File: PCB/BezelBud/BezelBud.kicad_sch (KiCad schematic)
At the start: 71 parts, among them J1 USB_C_Receptacle_USB2.0_16P, J2 Conn_01x05_Pin, SW1 SW_SPDT, SW2 SW_SPDT, SW3 SW_SPDT, SW4 SW_SPDT, SW5 SW_SPDT, SW6 SW_SPDT, SW7 SW_SPDT, SW8 SW_SPDT, SW9 SW_SPDT, U1 STM32G431CBT6, U2 USBLC6-2SC6, U3 LP5907MFX-3.3, U4 LP5907MFX-3.3, U5 PCM1861DBT, Y1 Crystal_GND24

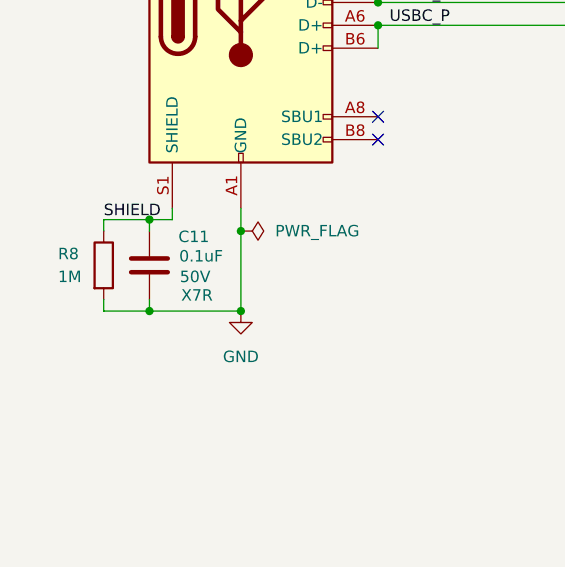
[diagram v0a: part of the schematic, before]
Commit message: removed usb decoupling and moved blink and led vias
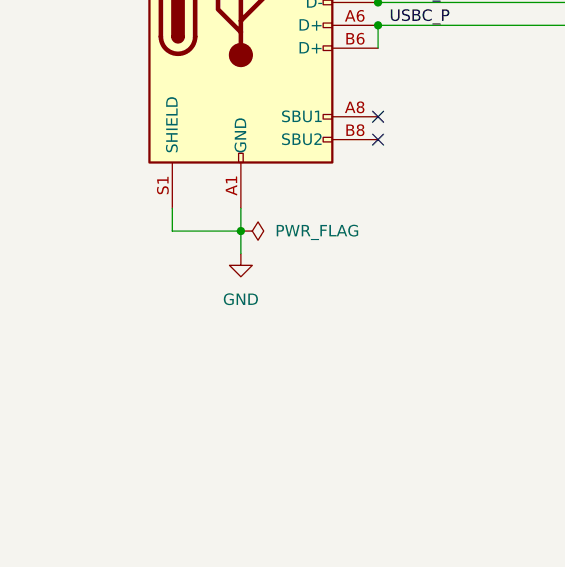
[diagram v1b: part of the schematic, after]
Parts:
- removed C11: 0.1uF, Capacitor_SMD:C_0603_1608Metric, symbol Device:C
- removed R8: 1M, Resistor_SMD:R_0603_1608Metric, symbol Device:R
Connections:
- net SHIELD is gone; now on net GND: J1.S1 (SHIELD)

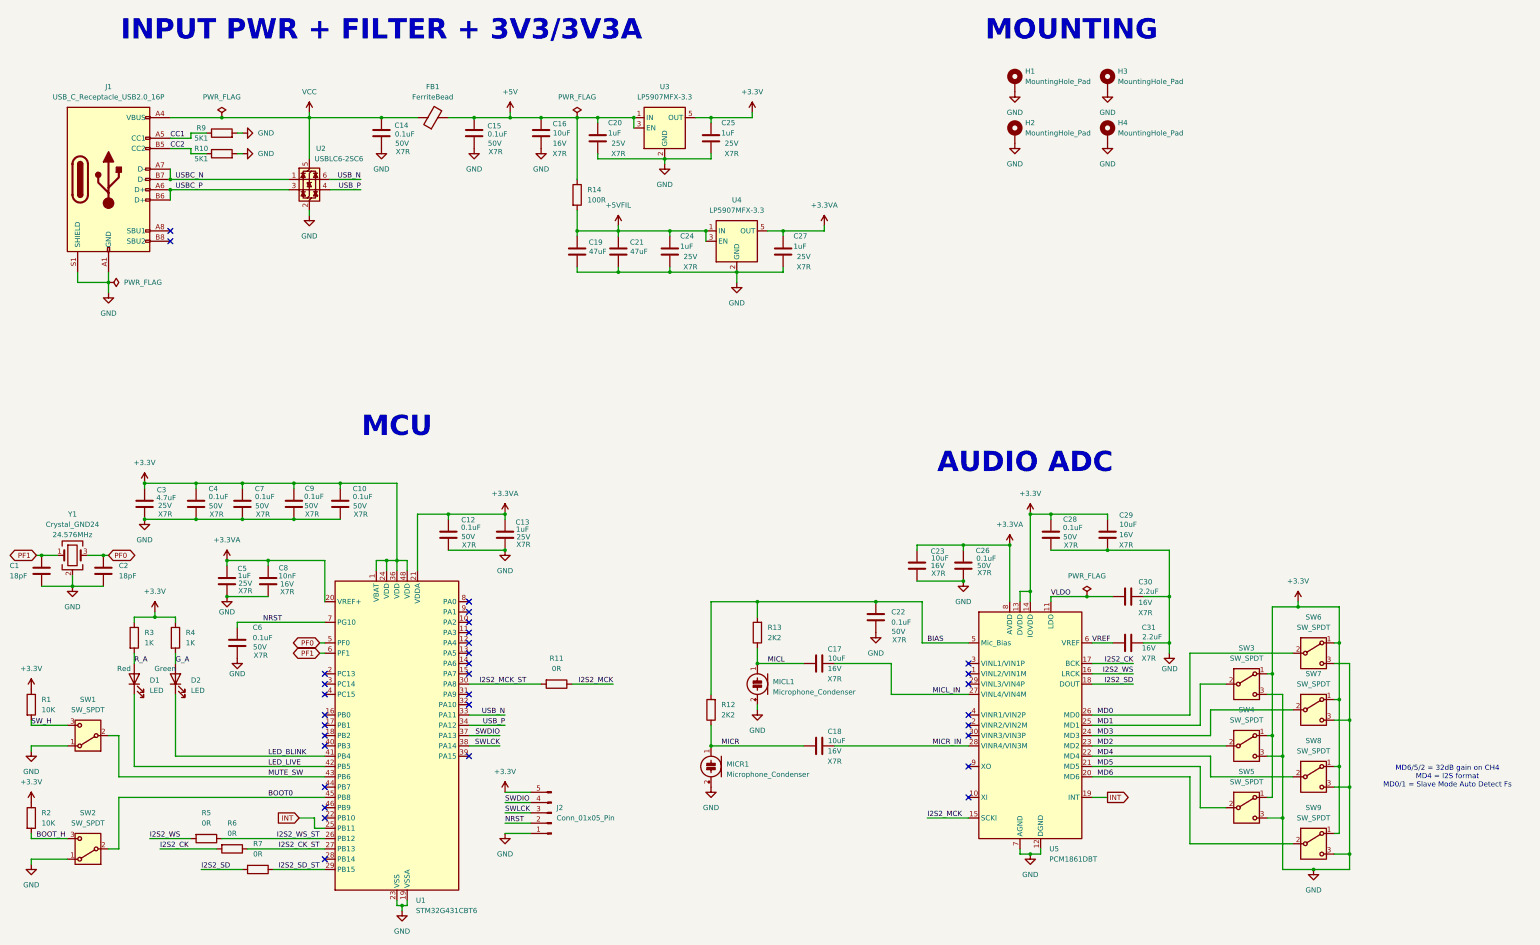
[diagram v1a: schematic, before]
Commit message: Updated to different Mic and finished PCB
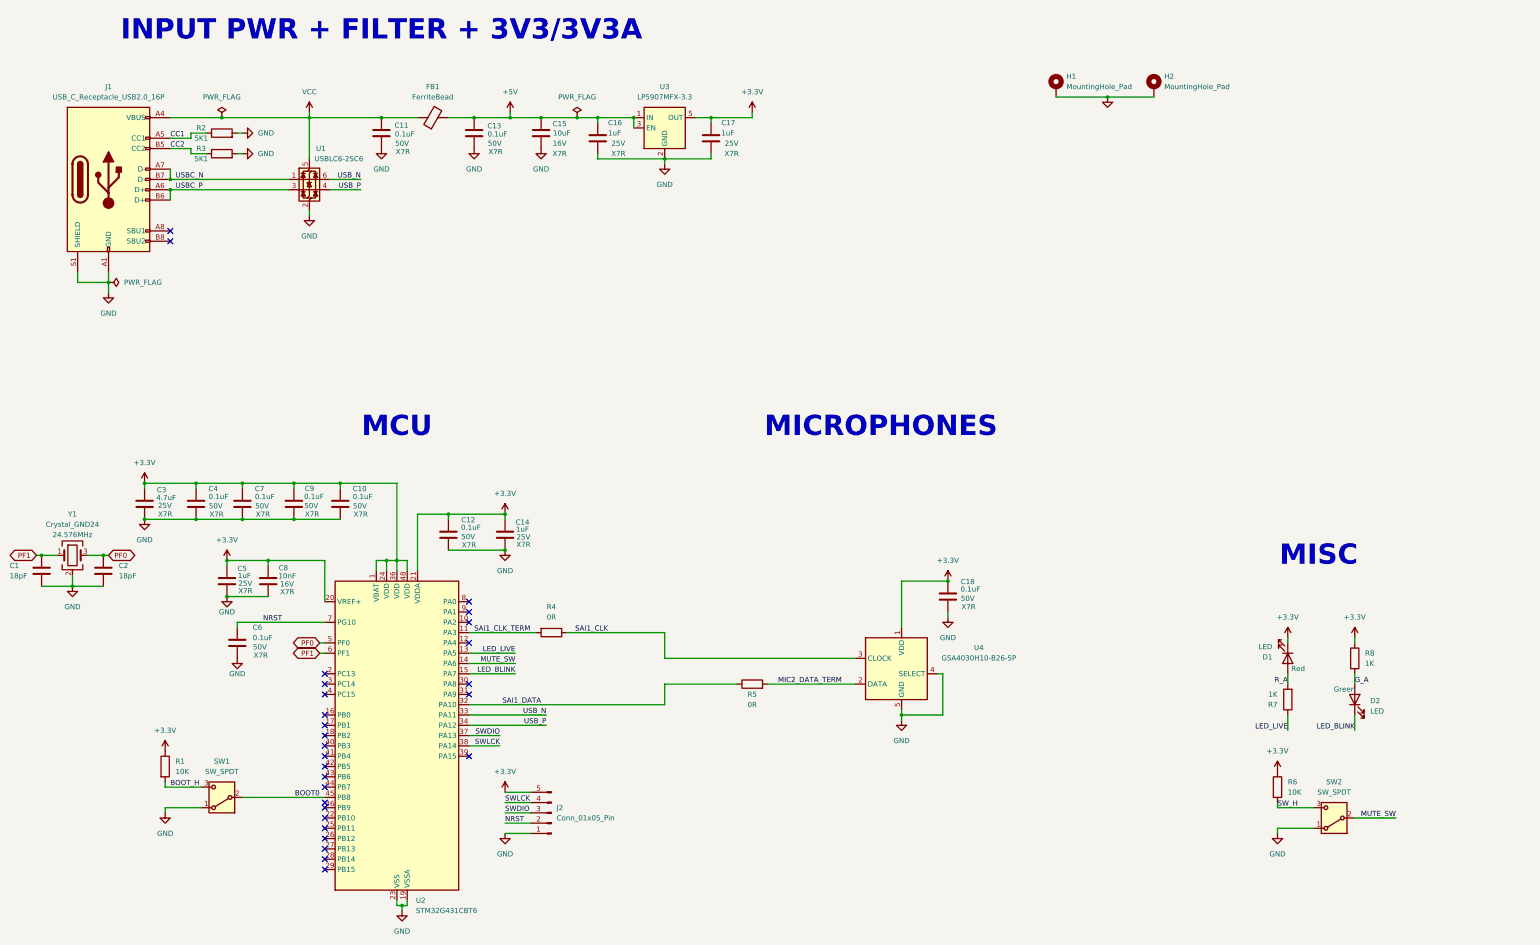
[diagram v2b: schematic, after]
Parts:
- removed C17, C23, C29: 10uF, Capacitor_SMD:C_0805_2012Metric, symbol Device:C
- removed C19, C21: 47uF, Capacitor_SMD:C_1206_3216Metric, symbol Device:C
- removed C22, C26, C28: 0.1uF, Capacitor_SMD:C_0603_1608Metric, symbol Device:C
- removed C24, C27: 1uF, Capacitor_SMD:C_0805_2012Metric, symbol Device:C
- removed C30, C31: 2.2uF, Capacitor_SMD:C_0603_1608Metric, symbol Device:C
- removed H3, H4: MountingHole_Pad, MountingHole:MountingHole_3.2mm_M3_Pad_Via, symbol Mechanical:MountingHole_Pad
- removed MICL1, MICR1: Microphone_Condenser, Resistor_THT:R_Axial_DIN0204_L3.6mm_D1.6mm_P1.90mm_Vertical, symbol Device:Microphone_Condenser
- removed R11, R6, R7: 0R, Resistor_SMD:R_0603_1608Metric, symbol Device:R
- removed R12, R13: 2K2, Resistor_SMD:R_0603_1608Metric, symbol Device:R
- removed R14: 100R, Resistor_SMD:R_0805_2012Metric, symbol Device:R
- removed R4: 1K, Resistor_SMD:R_0603_1608Metric, symbol Device:R
- removed SW3, SW4, SW5, SW6, SW7, SW8, SW9: SW_SPDT, Connector_PinHeader_2.54mm:PinHeader_1x03_P2.54mm_Vertical, symbol Switch:SW_SPDT
- removed U4: LP5907MFX-3.3, Package_TO_SOT_SMD:SOT-23-5, symbol Regulator_Linear:LP5907MFX-3.3
- removed U5: PCM1861DBT, Package_SO:TSSOP-30_4.4x7.8mm_P0.5mm, symbol Audio:PCM1860DBT
- added R5: 0R, Resistor_SMD:R_0603_1608Metric, symbol Device:R
- added R8: 1K, Resistor_SMD:R_0603_1608Metric, symbol Device:R
- added U4: GSA4030H10-B26-5P, BevelBud:GSA4030H10-B26-5P, symbol BevelBud:GSA4030H10-B26-5P
- C18: value 10uF -> 0.1uF; footprint Capacitor_SMD:C_0805_2012Metric -> Capacitor_SMD:C_0603_1608Metric; Voltage 16V -> 50V
- renumbered C14 to C11, C15 to C13, C13 to C14, C16 to C15, C20 to C16, C25 to C17, R2 to R1, R9 to R2, R10 to R3, R5 to R4, R1 to R6, R3 to R7, SW2 to SW1, SW1 to SW2, U2 to U1, U1 to U2
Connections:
- net +3.3VA is gone; now on net +3.3V: C12.1, C14.1, C5.1, C8.1, U2.20 (VREF+), U2.21 (VDDA)
- net I2S2_WS is gone; now on net SAI1_CLK_TERM: R4.2
- net MICR is gone; now on net +3.3V: C18.1
- net MICR_IN is gone; now on net GND: C18.2
- net +3.3V: now also D1.1 (K), R8.1, U4.1 (VDD); no longer R7.1
- net GND: now also U4.4 (SELECT), U4.5 (GND)
- net G_A: now also R8.2
- net LED_BLINK: now also U2.15 (PA7); no longer U2.41 (PB4)
- net LED_LIVE: now also R7.1, U2.13 (PA5); no longer D1.1 (K), U2.42 (PB5)
- net MUTE_SW: now also U2.14 (PA6); no longer U2.43 (PB6)
- net SWDIO: now also J2.3 (Pin_3); no longer J2.4 (Pin_4)
- net SWLCK: now also J2.4 (Pin_4); no longer J2.3 (Pin_3)
- net SAI1_CLK_TERM: now reaches U2.11 (PA3)
- net SAI1_DATA: now reaches U2.32 (PA10)
- net SAI1_DATA: now also R5.1
- net I2S2_CK_ST: no longer names the net of U2.27 (PB13)
- net I2S2_MCK_ST: no longer names the net of U2.30 (PA8)
- net I2S2_SD_ST: no longer names the net of U2.29 (PB15)
- net I2S2_WS_ST: no longer names the net of U2.26 (PB12)
- net I2S2_WS_ST: no longer R4.1
- net INT: no longer names the net of U2.25 (PB11)
- new net MIC2_DATA_TERM: R5.2, U4.2 (DATA)
- new net SAI1_CLK: R4.1, U4.3 (CLOCK)
- no-connect marks 32 -> 28
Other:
- note added: "MICROPHONES"
- note added: "MISC"
- note removed: "AUDIO ADC"
- note removed: "MD6/5/2 = 32dB gain on CH4 MD4 = I2S format MD0/1 = Slave Mode Auto Detect Fs"
- note removed: "MOUNTING"
- moved on the sheet: D1, R1, R4, R6, R7, SW1, SW2

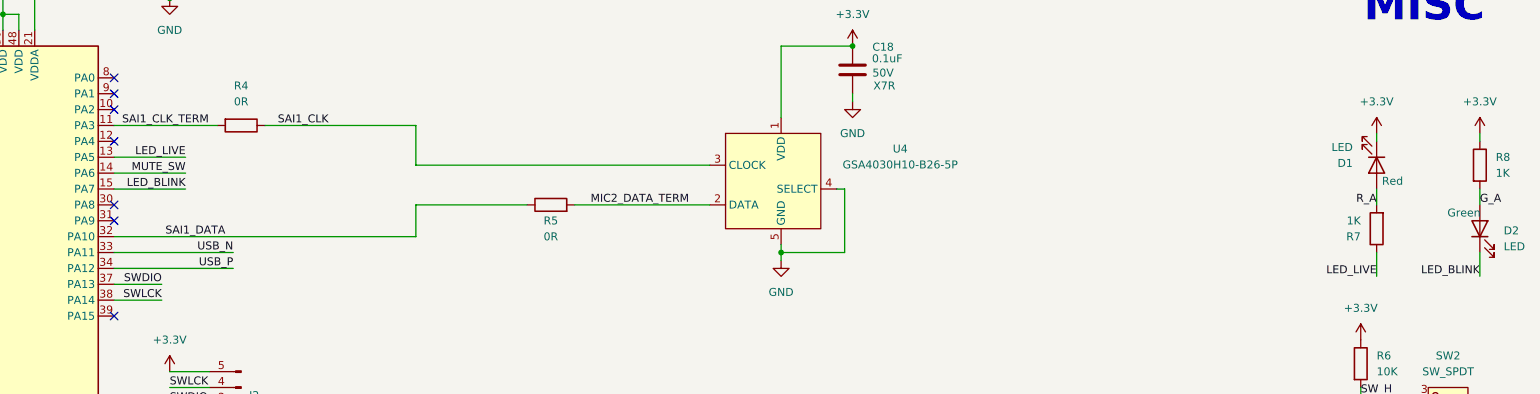
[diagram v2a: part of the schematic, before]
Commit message: deleted gerbers and fixed LED orientation
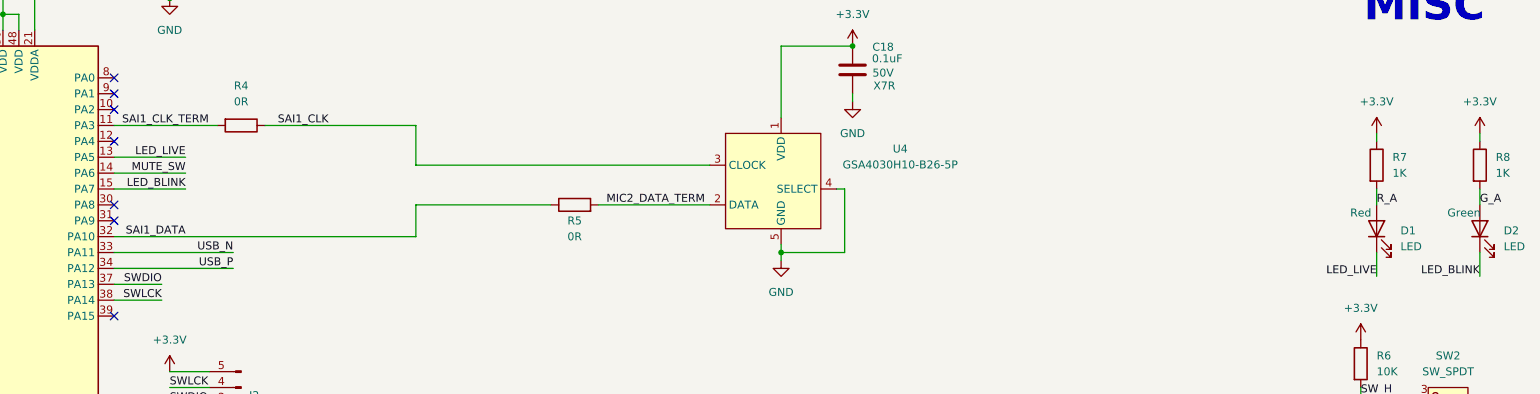
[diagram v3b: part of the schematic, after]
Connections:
- net +3.3V: now also R7.1; no longer D1.1 (K)
- net LED_LIVE: now also D1.1 (K); no longer R7.1
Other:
- moved on the sheet: D1, R5, R7
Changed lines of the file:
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@@
 	(wire
 		(pts
-			(xy 344.17 186.69) (xy 344.17 184.15)
+			(xy 344.17 184.15) (xy 344.17 186.69)
 		)
 		(stroke
@@
 	(wire
 		(pts
-			(xy 190.5 186.69) (xy 208.28 186.69)
+			(xy 190.5 186.69) (xy 212.09 186.69)
 		)
 		(stroke
@@
 	(wire
 		(pts
-			(xy 215.9 186.69) (xy 237.49 186.69)
+			(xy 219.71 186.69) (xy 237.49 186.69)
 		)
 		(stroke
@@
 	)
 	(label "SAI1_DATA"
-		(at 160.02 191.77 180)
+		(at 153.67 191.77 180)
 		(effects
 			(font
@@
 	)
 	(label "MIC2_DATA_TERM"
-		(at 218.44 186.69 0)
+		(at 220.98 186.69 0)
 		(effects
 			(font
@@
 	)
 	(label "R_A"
-		(at 344.17 186.69 180)
+		(at 344.17 186.69 0)
 		(effects
 			(font
 				(size 1.27 1.27)
 			)
-			(justify right bottom)
+			(justify left bottom)
 		)
 	)
@@
 	(symbol
 		(lib_id "Device:R")
-		(at 212.09 186.69 90)
+		(at 215.9 186.69 90)
 		(unit 1)
 		(exclude_from_sim no)
@@
 		(dnp no)
 		(property "Reference" "R5"
-			(at 212.09 189.23 90)
+			(at 215.9 189.23 90)
 			(effects
 				(font
@@
 		)
 		(property "Value" "0R"
-			(at 212.09 191.77 90)
+			(at 215.9 191.77 90)
 			(effects
 				(font
@@
 		)
 		(property "Footprint" "Resistor_SMD:R_0603_1608Metric"
-			(at 212.09 188.468 90)
+			(at 215.9 188.468 90)
 			(effects
 				(font
@@
 		)
 		(property "Datasheet" "~"
-			(at 212.09 186.69 0)
+			(at 215.9 186.69 0)
 			(effects
 				(font
@@
 		)
 		(property "Description" "Resistor"
-			(at 212.09 186.69 0)
+			(at 215.9 186.69 0)
 			(effects
 				(font
@@
 	(symbol
 		(lib_id "Device:R")
-		(at 344.17 190.5 180)
+		(at 344.17 180.34 0)
 		(unit 1)
 		(exclude_from_sim no)
@@
 		(fields_autoplaced yes)
 		(property "Reference" "R7"
-			(at 341.63 191.7701 0)
+			(at 346.71 179.0699 0)
 			(effects
 				(font
@@
 		)
 		(property "Value" "1K"
-			(at 341.63 189.2301 0)
+			(at 346.71 181.6099 0)
 			(effects
 				(font
@@
 		)
 		(property "Footprint" "Resistor_SMD:R_0603_1608Metric"
-			(at 345.948 190.5 90)
+			(at 342.392 180.34 90)
 			(effects
 				(font
@@
 		)
 		(property "Datasheet" "~"
-			(at 344.17 190.5 0)
+			(at 344.17 180.34 0)
 			(effects
 				(font
@@
 		)
 		(property "Description" "Resistor"
-			(at 344.17 190.5 0)
+			(at 344.17 180.34 0)
 			(effects
 				(font
@@
 	(symbol
 		(lib_id "Device:LED")
-		(at 344.17 180.34 270)
+		(at 344.17 190.5 90)
 		(unit 1)
 		(exclude_from_sim no)
@@
 		(dnp no)
 		(property "Reference" "D1"
-			(at 340.36 180.0226 90)
+			(at 347.98 190.8174 90)
 			(effects
 				(font
@@
 		)
 		(property "Value" "LED"
-			(at 340.36 177.4826 90)
+			(at 347.98 193.3574 90)
 			(effects
 				(font
@@
 		)
 		(property "Footprint" "LED_SMD:LED_0603_1608Metric"
-			(at 344.17 180.34 0)
+			(at 344.17 190.5 0)
 			(effects
 				(font
@@
 		)
 		(property "Datasheet" "~"
-			(at 344.17 180.34 0)
+			(at 344.17 190.5 0)
 			(effects
 				(font
@@
 		)
 		(property "Description" "Light emitting diode"
-			(at 344.17 180.34 0)
+			(at 344.17 190.5 0)
 			(effects
 				(font
@@
 		)
 		(property "Sim.Pins" "1=K 2=A"
-			(at 344.17 180.34 0)
+			(at 344.17 190.5 0)
 			(effects
 				(font
@@
 		)
 		(property "Colour" "Red"
-			(at 346.71 182.88 90)
+			(at 341.63 187.96 90)
 			(effects
 				(font
